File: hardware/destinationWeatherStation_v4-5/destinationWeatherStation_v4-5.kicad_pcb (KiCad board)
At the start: 2 copper layers, 63.5 x 50.8 mm, 39 parts, among them J1 S2B-PH-SM4, J2 MEM2061, J3 STEMMA_QT, Q1 IRLML6244TRPBF, Q2 IRLML6244TRPBF, Q3 DMP2035UVTQ-7, Q4 DMP2035UVTQ-7, SW1 SS-12F44-G5, SW2 PTS647SM38SMTR2LFS, SW3 PTS647SM38SMTR2LFS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

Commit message: fixing for final version
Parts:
- SW1: value SS-12F44-G5 -> OS102011MS2QN1; footprint lib_fp:SS-12D07-VG_GA_PA -> lib_fp:OS102011MS2QN1

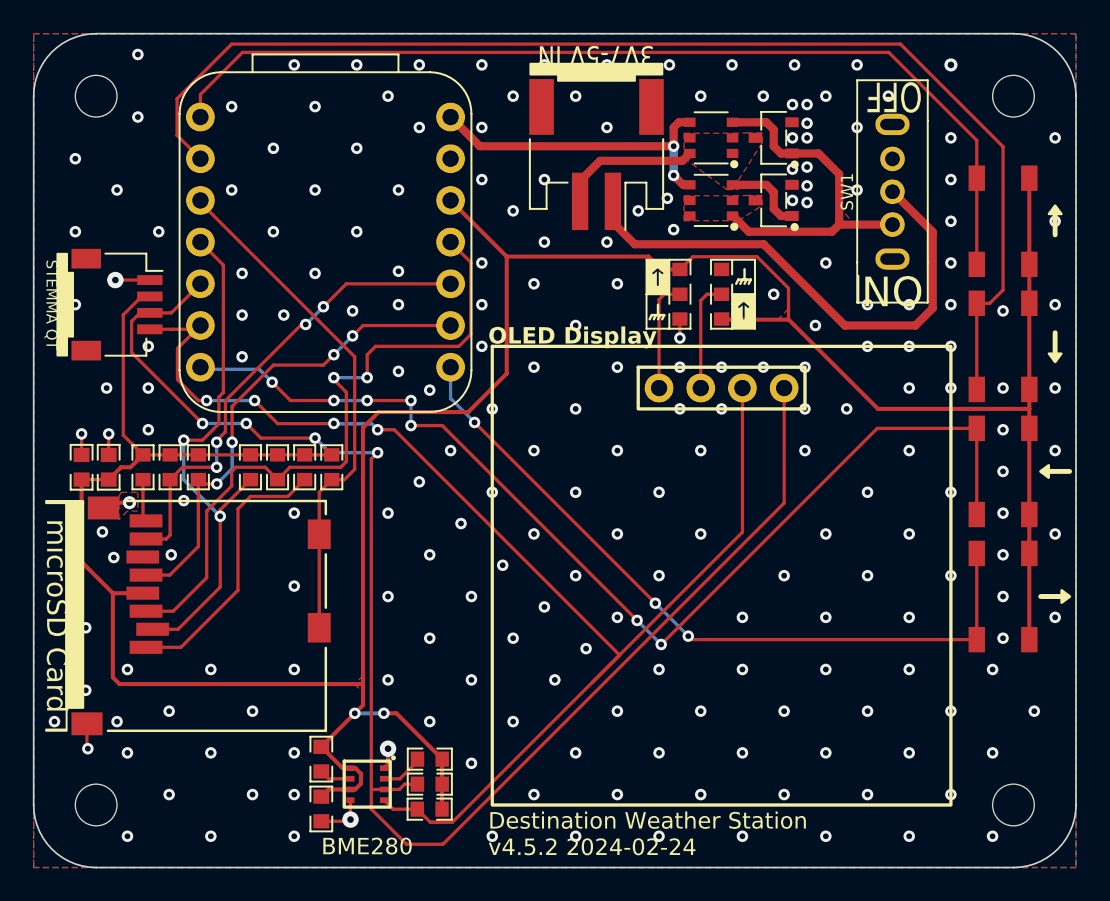
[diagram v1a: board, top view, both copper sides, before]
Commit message: nudged traces and relinked footprints and models
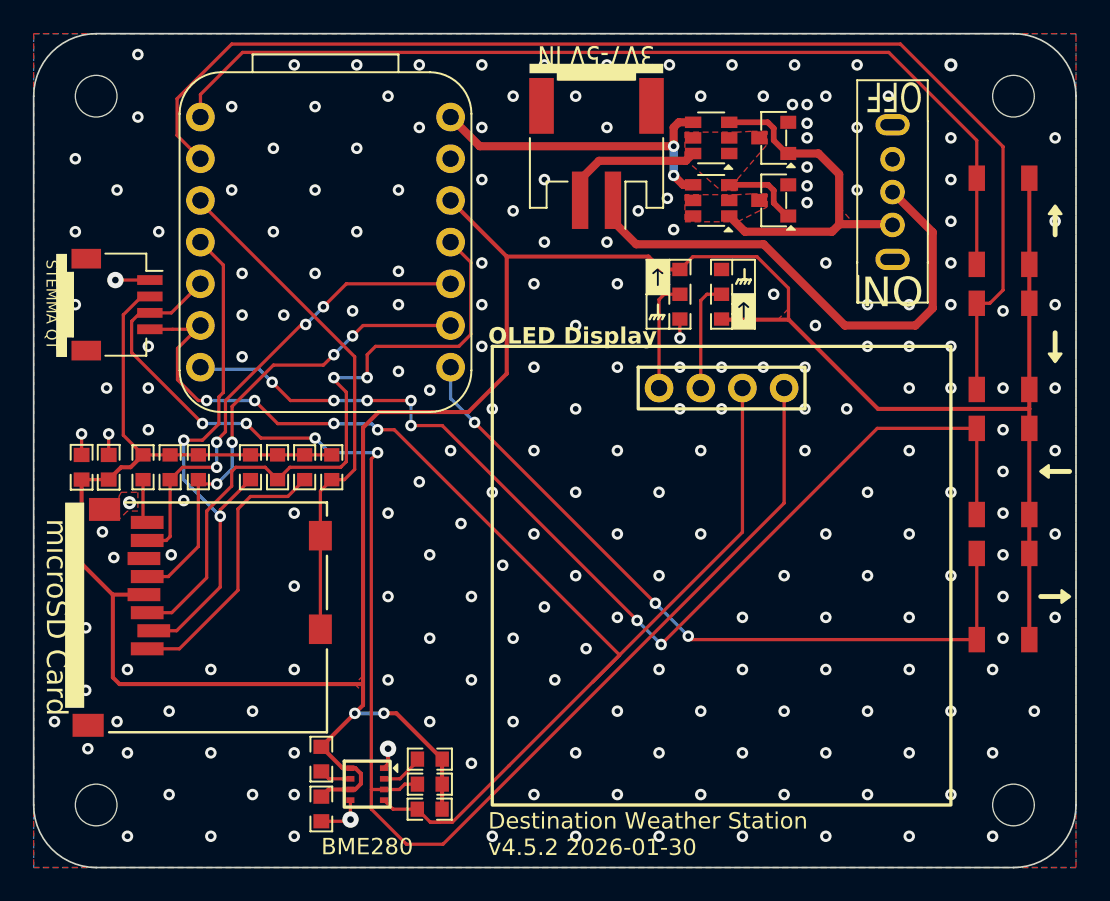
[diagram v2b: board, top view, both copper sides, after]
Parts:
- moved J2 0.11 mm to (117.3, 106.7)
- moved J1 0.07 mm to (147.3, 77.5)
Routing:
- net GND: track 15.5 -> 12.4 mm, vias 223 -> 220
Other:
- board text added: "Destination Weather Station v4.5.2 2026-01-30"
- board text removed: "Destination Weather Station v4.5.2 2024-02-24"
- board text removed: "PCB3D_BR_DS-WX-STN-v4-5"
- board text removed: "PCB3D_TL_DS-WX-STN-v4-5"

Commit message: changes
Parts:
- moved J2 6.35 mm to (123.7, 106.7)
- moved J1 0.89 mm to (147.3, 78.4)
- moved R11 0.76 mm to (152.4, 86.2)
- moved R12 0.76 mm to (154.9, 86.2)
- turned Q1 to 0 degrees
- turned Q2 to 0 degrees
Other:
- board text added: "Destination Weather Station v4.5.2 2026-02-02"
- board text removed: "Destination Weather Station v4.5.2 2026-01-30"

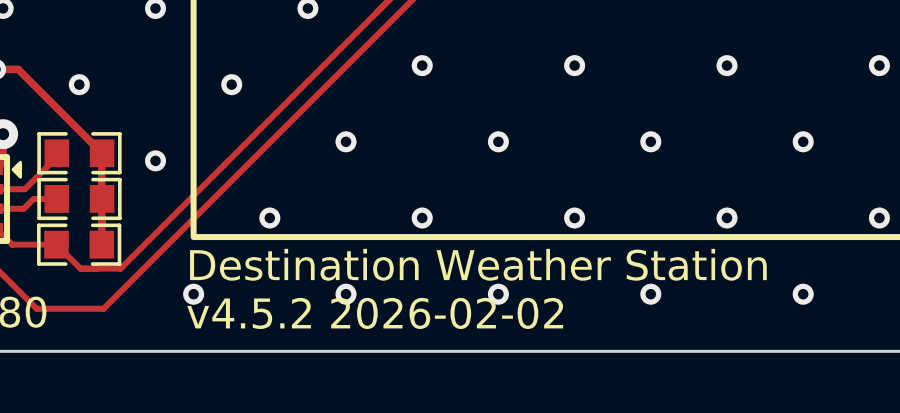
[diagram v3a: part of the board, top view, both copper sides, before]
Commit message: updated silkscreen and fixed copper pours
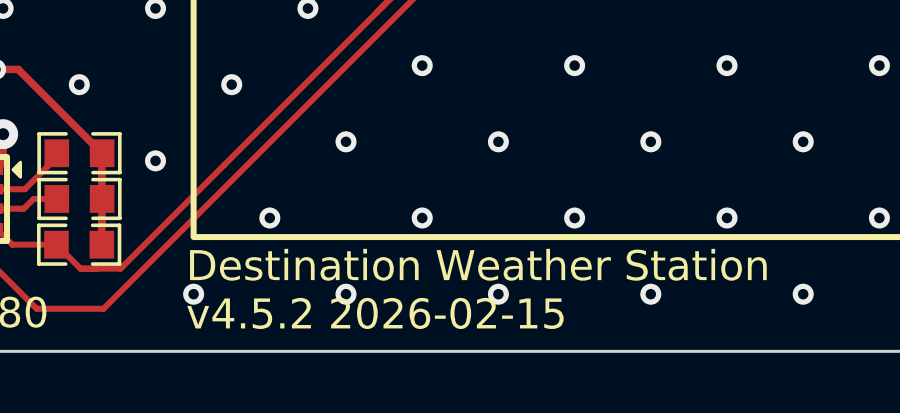
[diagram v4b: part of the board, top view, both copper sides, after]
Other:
- board text added: "Destination Weather Station v4.5.2 2026-02-15"
- board text removed: "Destination Weather Station v4.5.2 2026-02-02"
